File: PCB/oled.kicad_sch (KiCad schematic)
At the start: 3 parts

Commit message: fix: swap 3 JLCPCB-out-of-stock parts for in-stock equivalents
C_BAT1/C_BUCK_IN1/C_OLED_1/C_SYS_1/C_VIN_1 (10uF 0805 X5R 16V):
Yageo CC0805KRX5R7BB106 was at 0 stock -> HRE CGA0805X5R106K160MT
(LCSC C6119886, stock ~254k). Identical spec, different brand.

D_VBUS_TVS1: Nexperia PESD5V0S1BA,115 was down to 1 in stock -> TECH
PUBLIC TPPESD5V0S1BA (LCSC C587144, stock ~981k), a widely-stocked
pin/spec-compatible clone of the same part, same SOD-323 package.

Q_PWR1: Diodes Inc DMG2305UX-7 was down to 8 in stock -> Diodes Inc
DMG2305UX-13 (LCSC C144153, stock ~25k) -- same manufacturer, same
part, the -7/-13 suffix is just reel size (7"/13"), not an electrical
variant.

Found via live JLCPCB stock lookups after the JLCPCB upload flagged
these 3 with shortfalls. Verified via kicad-cli sch export bom and
sch erc (0 violations).

Note: PCB/snips_controller.kicad_pcb and the production/ exports still
need another Update-PCB-from-Schematic + Fabrication Toolkit pass to
pick up these changes -- not included here since they're a separate
manual step (see kicad_pcb_sync_gotcha note).

Co-Authored-By: Claude Sonnet 5 <noreply@anthropic.com>
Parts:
- C_OLED_1: LCSC C2982567 -> C6119886; MF Yageo -> HRE; Manufacturer_Part_Number CC0805KRX5R7BB106 -> CGA0805X5R106K160MT
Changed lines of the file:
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@@
 			)
 		)
-		(property "MF" "Yageo"
+		(property "MF" "HRE"
 			(at 0 0 0)
 			(hide yes)
@@
 			)
 		)
-		(property "Manufacturer_Part_Number" "CC0805KRX5R7BB106"
+		(property "Manufacturer_Part_Number" "CGA0805X5R106K160MT"
 			(at 0 0 0)
 			(hide yes)
@@
 			)
 		)
-		(property "LCSC" "C2982567"
+		(property "LCSC" "C6119886"
 			(at 0 0 0)
 			(hide yes)

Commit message: task: alert on Basic-library alternatives during JLC part matching (#33)
* task: alert on Basic-library alternatives during JLC part matching

JLC's "Extended" library carries a per-unique-part setup fee on top of
unit price; "Basic" doesn't. That fee doesn't amortize well on a board
with many distinct low-quantity parts -- confirmed the hard way: our
first real JLCPCB assembly quote came back at $333.84 vs PCBWay's
~$190 for the same order, and all 33 of our matched parts were
Extended.

jlc_match.py now does a secondary search for a same-value/same-package
Basic-library part whenever the real match lands on Extended, and
flags it in the report (new BasicAlt column + a Status alert) rather
than silently leaving it. On the current board this surfaces 11
plausible Basic-library swaps (common resistor/cap values, and the
generic 1N4148W diode and 2N7002 MOSFET, which are industry-standard
parts many brands stock identically).

This is alert-only, same as the rest of this script -- it doesn't
touch the schematic. Spot-checked 4 of the 11 suggestions directly
against JLC's catalog to confirm value/package actually match, not
just a keyword hit.

Co-Authored-By: Claude Sonnet 5 <noreply@anthropic.com>

* fix: two correctness bugs in Basic-library alternative matching

1. find_basic_alternative() trusted the raw keyword-search hit without
   verifying the candidate's actual value -- JLC's fuzzy full-text search
   can return a wrong-value part that just shares digits (e.g. searching
   "100 0402" surfaced a 1kΩ resistor, EIA code "1001", as a false match
   for a 100Ω part). Now parses and compares the actual numeric value
   (with unit) before accepting a candidate; falls back to exact
   model-name matching for non-numeric values (generic diode/transistor
   part families like "1N4148W", "2N7002").

2. The new value parser's regex required the unit to be the first
   character of the string, but JLC resistor descriptions carry a
   Chinese prefix ("厚膜电阻 10kΩ ±1%" = "thi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
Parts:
- C_OLED_1: LCSC C6119886 -> C15850; MF HRE -> Samsung Electro-Mechanics; Manufacturer_Part_Number CGA0805X5R106K160MT -> CL21A106KAYNNNE
- C_OLED_2: LCSC C131394 -> C1525; MF Yageo -> Samsung Electro-Mechanics; Manufacturer_Part_Number CC0402KRX7R9BB104 -> CL05B104KO5NNNC
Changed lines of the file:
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@@
 			)
 		)
-		(property "MF" "HRE"
+		(property "MF" "Samsung Electro-Mechanics"
 			(at 0 0 0)
 			(hide yes)
@@
 			)
 		)
-		(property "Manufacturer_Part_Number" "CGA0805X5R106K160MT"
+		(property "Manufacturer_Part_Number" "CL21A106KAYNNNE"
 			(at 0 0 0)
 			(hide yes)
@@
 			)
 		)
-		(property "LCSC" "C6119886"
+		(property "LCSC" "C15850"
 			(at 0 0 0)
 			(hide yes)
@@
 			)
 		)
-		(property "MF" "Yageo"
+		(property "MF" "Samsung Electro-Mechanics"
 			(at 0 0 0)
 			(hide yes)
@@
 			)
 		)
-		(property "Manufacturer_Part_Number" "CC0402KRX7R9BB104"
+		(property "Manufacturer_Part_Number" "CL05B104KO5NNNC"
 			(at 0 0 0)
 			(hide yes)
@@
 			)
 		)
-		(property "LCSC" "C131394"
+		(property "LCSC" "C1525"
 			(at 0 0 0)
 			(hide yes)

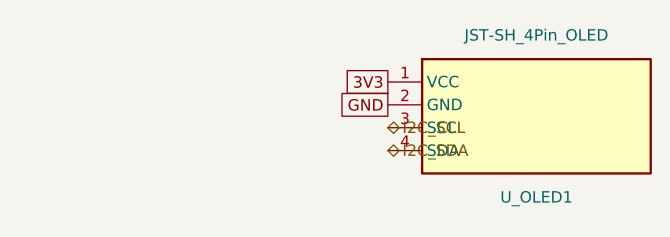
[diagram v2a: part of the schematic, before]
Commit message: fix: resolve first-board bring-up issues (power, OLED, XBee diagnostics, button naming) (#53)
Found and fixed during hands-on bring-up of the first assembled board:

- Power-button-sense polarity was inverted (assumed active-high, actually
  active-low via an external pull-up) -- read the button as continuously
  held from boot and triggered an unwanted graceful shutdown 3s into every
  session.
- OledDisplay could crash (StoreProhibited/null-buffer write) whenever the
  display wasn't present, because Adafruit_SSD1306::begin() never
  allocates its frame buffer unless its own begin() is called, and nothing
  else in the call chain checked readiness before rendering. Added a real
  I2C presence check (Adafruit's begin() never actually verifies an ACK)
  with fallback between 0x3C/0x3D, a full bus-scan diagnostic on total
  failure, and a readiness guard on every OledDisplay method.
- Serial never reached the USB port at all: this board has no external
  USB-UART bridge, and ARDUINO_USB_CDC_ON_BOOT wasn't set, so Serial was
  going to unconnected UART0 pins instead of the native USB-CDC port.
- Early boot diagnostics were getting lost even with a monitor already
  open, because native USB-CDC has to re-enumerate with the host after
  every reset. Added a bounded wait for an actual host connection before
  continuing.
- Added an XBee ATTN pin read at boot to help isolate SPI wiring issues
  from module/firmware issues.
- Buttons::kLeftUp/kLeftDown and kRightUp/kRightDown were mapped to the
  physically wrong button pairs (Vol/Trigger swapped) -- confirmed against
  the real controller and corrected.
- The Button Test screen never updated after the first button press --
  the display's change-detection only watched currentScreen()/
  selectedMainMenuItem(), not lastTestedButtonIndex(), so pressing a
  button while already on that screen never triggered a redraw.
- KiCad: the OLED Qwiic connector's pin assignment in
  SnipsControllers:SSD1306_OLED_4pin was wrong on two 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
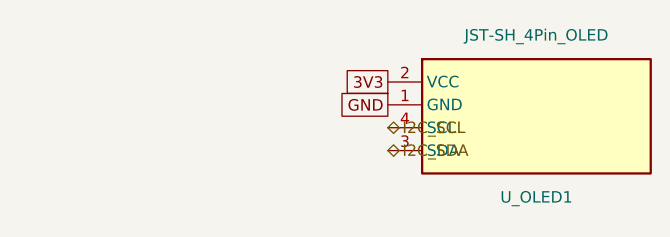
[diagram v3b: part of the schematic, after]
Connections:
- net 3V3: now also U_OLED1.2 (VCC); no longer U_OLED1.1 (VCC)
- net GND: now also U_OLED1.1 (GND); no longer U_OLED1.2 (GND)
- net I2C_SCL: now also U_OLED1.4 (SCL); no longer U_OLED1.3 (SCL)
- net I2C_SDA: now also U_OLED1.3 (SDA); no longer U_OLED1.4 (SDA)

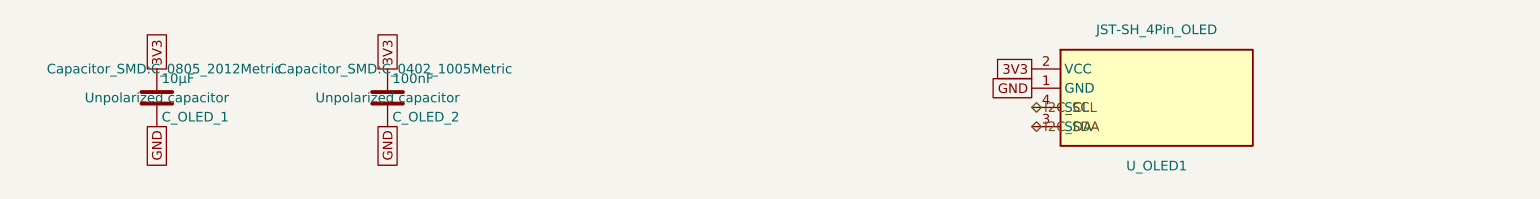
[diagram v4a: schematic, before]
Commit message: fix: make every BOM Value unambiguous for the fab, and switch D_INV_ISO1 to SOT-323 (#61)
* fix: make every BOM Value unambiguous for the fab, and switch D_INV_ISO1 to SOT-323

PCBWay flagged D_INV_ISO1: "BAT54W" is SOT-323 from nearly every maker, but we
had picked Yangjie's SOD-123 variant. A fab only sees Designator, Footprint,
Quantity and Value in the BOM (never MF/MPN/LCSC), so a bare part name is
ambiguous. Fixes the class of problem, not just this part:

- Every component's Value is now "<label> | <MPN> | <manufacturer> | <package>"
  (label dropped when it repeats the MPN; commas/periods stripped so the CSV
  never needs quoting). BT1 keeps its RIGHT-ANGLE HORIZONTAL note. Applied to
  all 81 parts across every sheet and the PCB.
- scripts/bom_values.py builds, applies, and checks these values, including
  that the PCB copy of Value/MF/MPN/footprint matches the schematic. New
  footprints must be added to its package table on purpose; hand-sourced parts
  with no MPN (J_STICK1) are listed explicitly.
- D_INV_ISO1 -> Diodes BAT54W-7-F in SOT-323 (common part, several makers).
  Pin 1 anode / pin 2 not connected / pin 3 cathode, confirmed against
  Nexperia's numbered pinning table and Diodes' datasheet. Uses KiCad's
  Diode:BAT54W symbol; PCB footprint replaced and rerouted. Electrically the
  same BAT54 family (30V, 200mA, 2uA leakage at 25V), so the SPICE model and
  scripts/spice/latch_sim.py still pass.
- Layout diagrams now say AO3401A for Q_PWR1 (they were stale since it was
  swapped from DMG2305UX) and BAT54W-7-F/SOT-323 for D_INV_ISO1.
- Repo CLAUDE.md documents the Value rule and the script.

ERC/DRC clean; production files regenerated.

Co-Authored-By: Claude Sonnet 5 <noreply@anthropic.com>

* chore: commit KiCad project settings (reordered used-designators list)

Co-Authored-By: Claude Sonnet 5 <noreply@anthropic.com>

---------

Co-authored-by: Claude Sonnet 5 <noreply@anthropic.com>
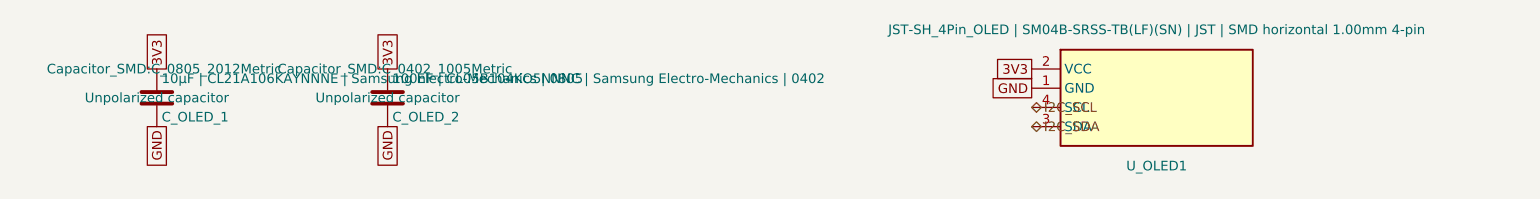
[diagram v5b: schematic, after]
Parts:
- C_OLED_1: value 10µF -> 10µF | CL21A106KAYNNNE | Samsung Electro-Mechanics | 0805
- C_OLED_2: value 100nF -> 100nF | CL05B104KO5NNNC | Samsung Electro-Mechanics | 0402
- U_OLED1: value JST-SH_4Pin_OLED -> JST-SH_4Pin_OLED | SM04B-SRSS-TB(LF)(SN) | JST | SMD horizontal 1.00mm 4-pin
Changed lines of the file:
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@@
 			)
 		)
-		(property "Value" "JST-SH_4Pin_OLED"
+		(property "Value" "JST-SH_4Pin_OLED | SM04B-SRSS-TB(LF)(SN) | JST | SMD horizontal 1.00mm 4-pin"
 			(at 214.63 96.41 0)
 			(show_name no)
@@
 			)
 		)
-		(property "Value" "10µF"
+		(property "Value" "10µF | CL21A106KAYNNNE | Samsung Electro-Mechanics | 0805"
 			(at 83.185 102.87 0)
 			(show_name no)
@@
 			)
 		)
-		(property "Value" "100nF"
+		(property "Value" "100nF | CL05B104KO5NNNC | Samsung Electro-Mechanics | 0402"
 			(at 113.665 102.87 0)
 			(show_name no)
